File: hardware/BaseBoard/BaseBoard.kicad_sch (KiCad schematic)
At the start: 79 parts, among them IC1 PCF8574RGTR, J1-ESP1 ESP-1-L, J1-ESP2 ESP-1-L, J1-ESP3 ESP-1-L, J1-ESP4 ESP-1-L, J1-ESP5 ESP-1-L, J1-ESP6 ESP-1-L, J1-ESP7 ESP-1-L, J1-ESP8 ESP-1-L, J2-ESP1 ESP-1-R, J2-ESP2 ESP-1-R, J2-ESP3 ESP-1-R, J2-ESP4 ESP-1-R, J2-ESP5 ESP-1-R, J2-ESP6 ESP-1-R, J2-ESP7 ESP-1-R, J2-ESP8 ESP-1-R, J3-BUS1 BUS-IN, J3-BUS2 BUS-IN, J3-BUS3 BUS-IN, J3-BUS4 BUS-IN, J3-BUS5 BUS-IN, J3-BUS6 BUS-IN, J3-BUS7 BUS-IN, J3-BUS8 BUS-IN, J4-BUS1 BUS-OUT, J4-BUS2 BUS-OUT, J4-BUS3 BUS-OUT, J4-BUS4 BUS-OUT, J4-BUS5 BUS-OUT, J4-BUS6 BUS-OUT, J4-BUS7 BUS-OUT, J4-BUS8 BUS-OUT, Q1 AO3401A, Q2 AO3401A, Q3 AO3401A, Q4 AO3401A, Q5 AO3401A, Q6 AO3401A, Q7 AO3401A, Q8 AO3401A, SW1 SW_DIP_SPSTx03

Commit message: Larger resistors and more GND vias.
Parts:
- R11, R12, R21, R22, R31, R32, R41, R42, R51, R52, R61, R62, R71, R72, R81, R82: footprint Resistor_SMD:R_0402_1005Metric -> Resistor_SMD:R_0805_2012Metric
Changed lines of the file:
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@@
 			)
 		)
-		(property "Footprint" "Resistor_SMD:R_0402_1005Metric"
+		(property "Footprint" "Resistor_SMD:R_0805_2012Metric"
 			(at 66.548 77.47 90)
 			(effects
@@
 			)
 		)
-		(property "Footprint" "Resistor_SMD:R_0402_1005Metric"
+		(property "Footprint" "Resistor_SMD:R_0805_2012Metric"
 			(at 59.69 84.328 90)
 			(effects
@@
 			)
 		)
-		(property "Footprint" "Resistor_SMD:R_0402_1005Metric"
+		(property "Footprint" "Resistor_SMD:R_0805_2012Metric"
 			(at 130.81 44.958 90)
 			(effects
@@
 			)
 		)
-		(property "Footprint" "Resistor_SMD:R_0402_1005Metric"
+		(property "Footprint" "Resistor_SMD:R_0805_2012Metric"
 			(at 130.81 84.328 90)
 			(effects
@@
 			)
 		)
-		(property "Footprint" "Resistor_SMD:R_0402_1005Metric"
+		(property "Footprint" "Resistor_SMD:R_0805_2012Metric"
 			(at 59.69 44.958 90)
 			(effects
@@
 			)
 		)
-		(property "Footprint" "Resistor_SMD:R_0402_1005Metric"
+		(property "Footprint" "Resistor_SMD:R_0805_2012Metric"
 			(at 137.668 116.84 90)
 			(effects
@@
 			)
 		)
-		(property "Footprint" "Resistor_SMD:R_0402_1005Metric"
+		(property "Footprint" "Resistor_SMD:R_0805_2012Metric"
 			(at 130.81 123.698 90)
 			(effects
@@
 			)
 		)
-		(property "Footprint" "Resistor_SMD:R_0402_1005Metric"
+		(property "Footprint" "Resistor_SMD:R_0805_2012Metric"
 			(at 130.81 163.068 90)
 			(effects
@@
 			)
 		)
-		(property "Footprint" "Resistor_SMD:R_0402_1005Metric"
+		(property "Footprint" "Resistor_SMD:R_0805_2012Metric"
 			(at 59.69 123.698 90)
 			(effects
@@
 			)
 		)
-		(property "Footprint" "Resistor_SMD:R_0402_1005Metric"
+		(property "Footprint" "Resistor_SMD:R_0805_2012Metric"
 			(at 66.548 156.21 90)
 			(effects
@@
 			)
 		)
-		(property "Footprint" "Resistor_SMD:R_0402_1005Metric"
+		(property "Footprint" "Resistor_SMD:R_0805_2012Metric"
 			(at 66.548 38.1 90)
 			(effects
@@
 			)
 		)
-		(property "Footprint" "Resistor_SMD:R_0402_1005Metric"
+		(property "Footprint" "Resistor_SMD:R_0805_2012Metric"
 			(at 137.668 156.21 90)
 			(effects
@@
 			)
 		)
-		(property "Footprint" "Resistor_SMD:R_0402_1005Metric"
+		(property "Footprint" "Resistor_SMD:R_0805_2012Metric"
 			(at 59.69 163.068 90)
 			(effects
@@
 			)
 		)
-		(property "Footprint" "Resistor_SMD:R_0402_1005Metric"
+		(property "Footprint" "Resistor_SMD:R_0805_2012Metric"
 			(at 137.668 38.1 90)
 			(effects
@@
 			)
 		)
-		(property "Footprint" "Resistor_SMD:R_0402_1005Metric"
+		(property "Footprint" "Resistor_SMD:R_0805_2012Metric"
 			(at 137.668 77.47 90)
 			(effects
@@
 			)
 		)
-		(property "Footprint" "Resistor_SMD:R_0402_1005Metric"
+		(property "Footprint" "Resistor_SMD:R_0805_2012Metric"
 			(at 66.548 116.84 90)
 			(effects

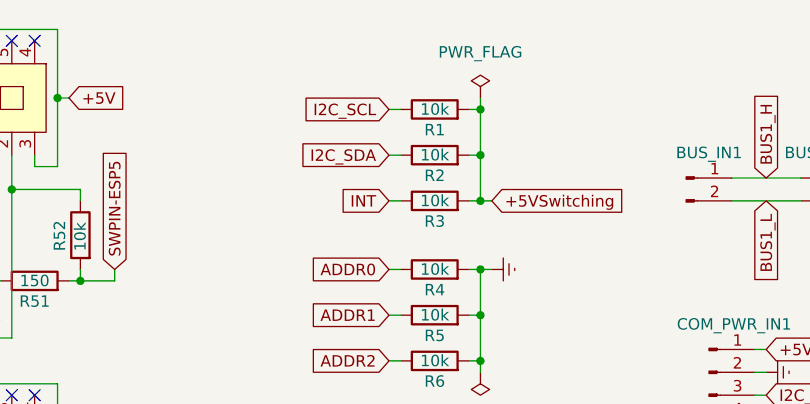
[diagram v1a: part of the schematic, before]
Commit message: Removed pull-up resistors for I2C slaves.
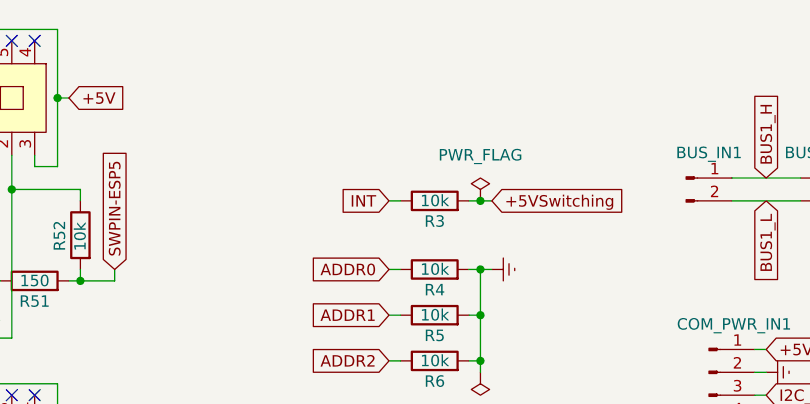
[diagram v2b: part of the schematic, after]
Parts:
- removed R1, R2: 10k, Resistor_SMD:R_0402_1005Metric, symbol Device:R

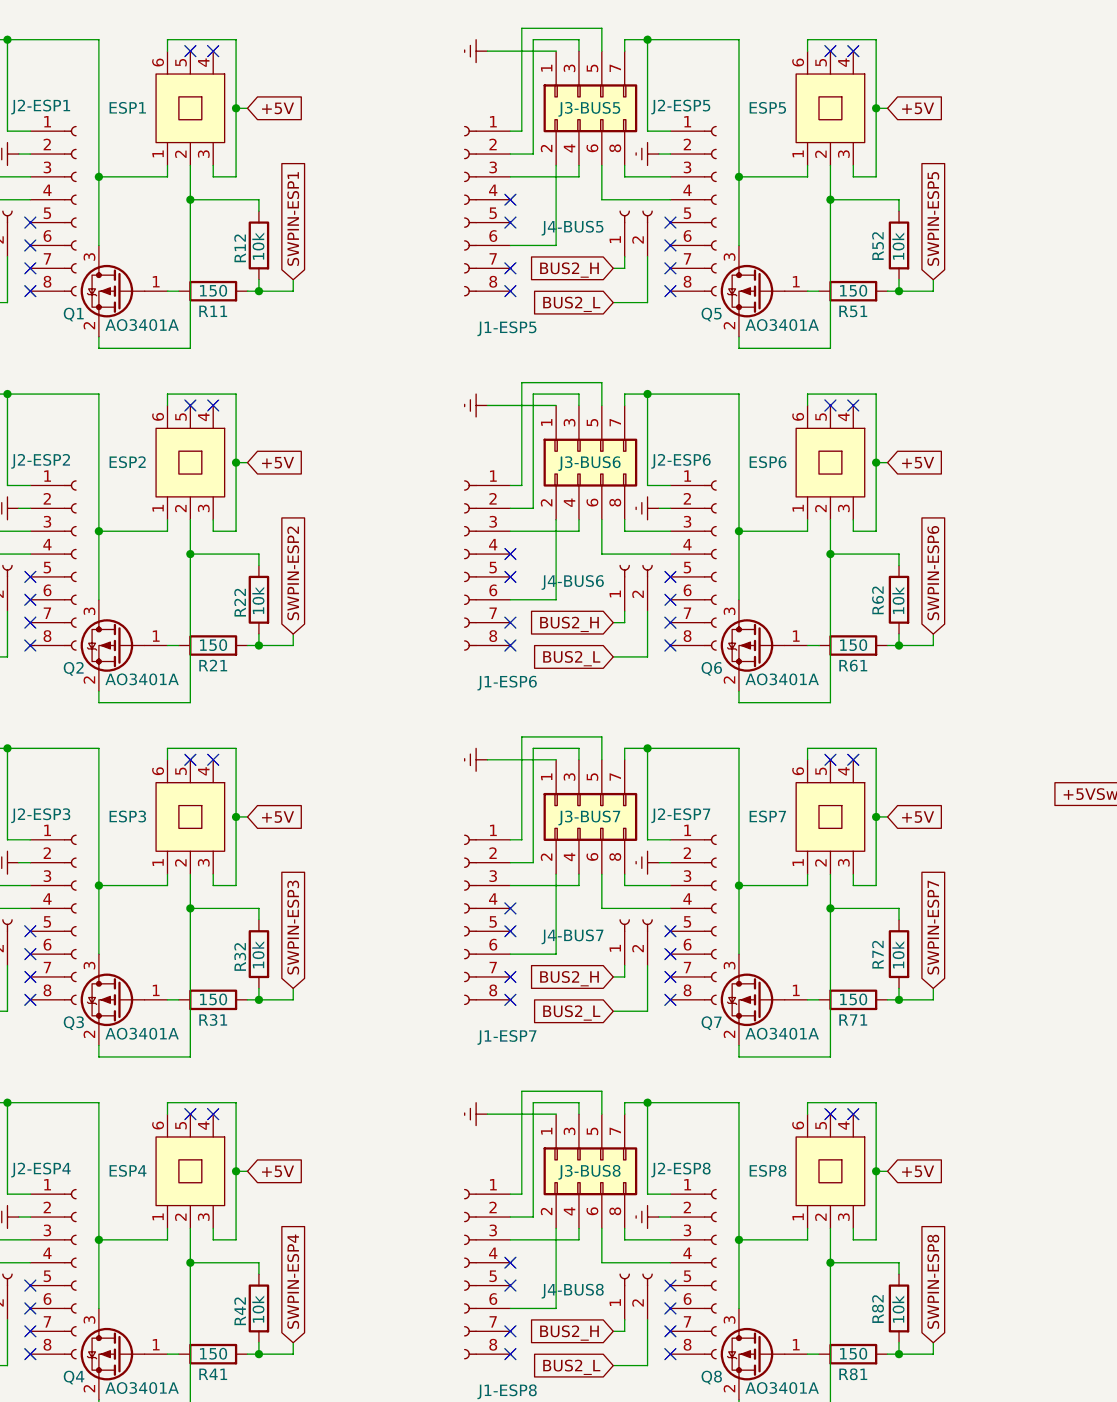
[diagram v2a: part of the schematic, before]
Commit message: Added diodes to base board.
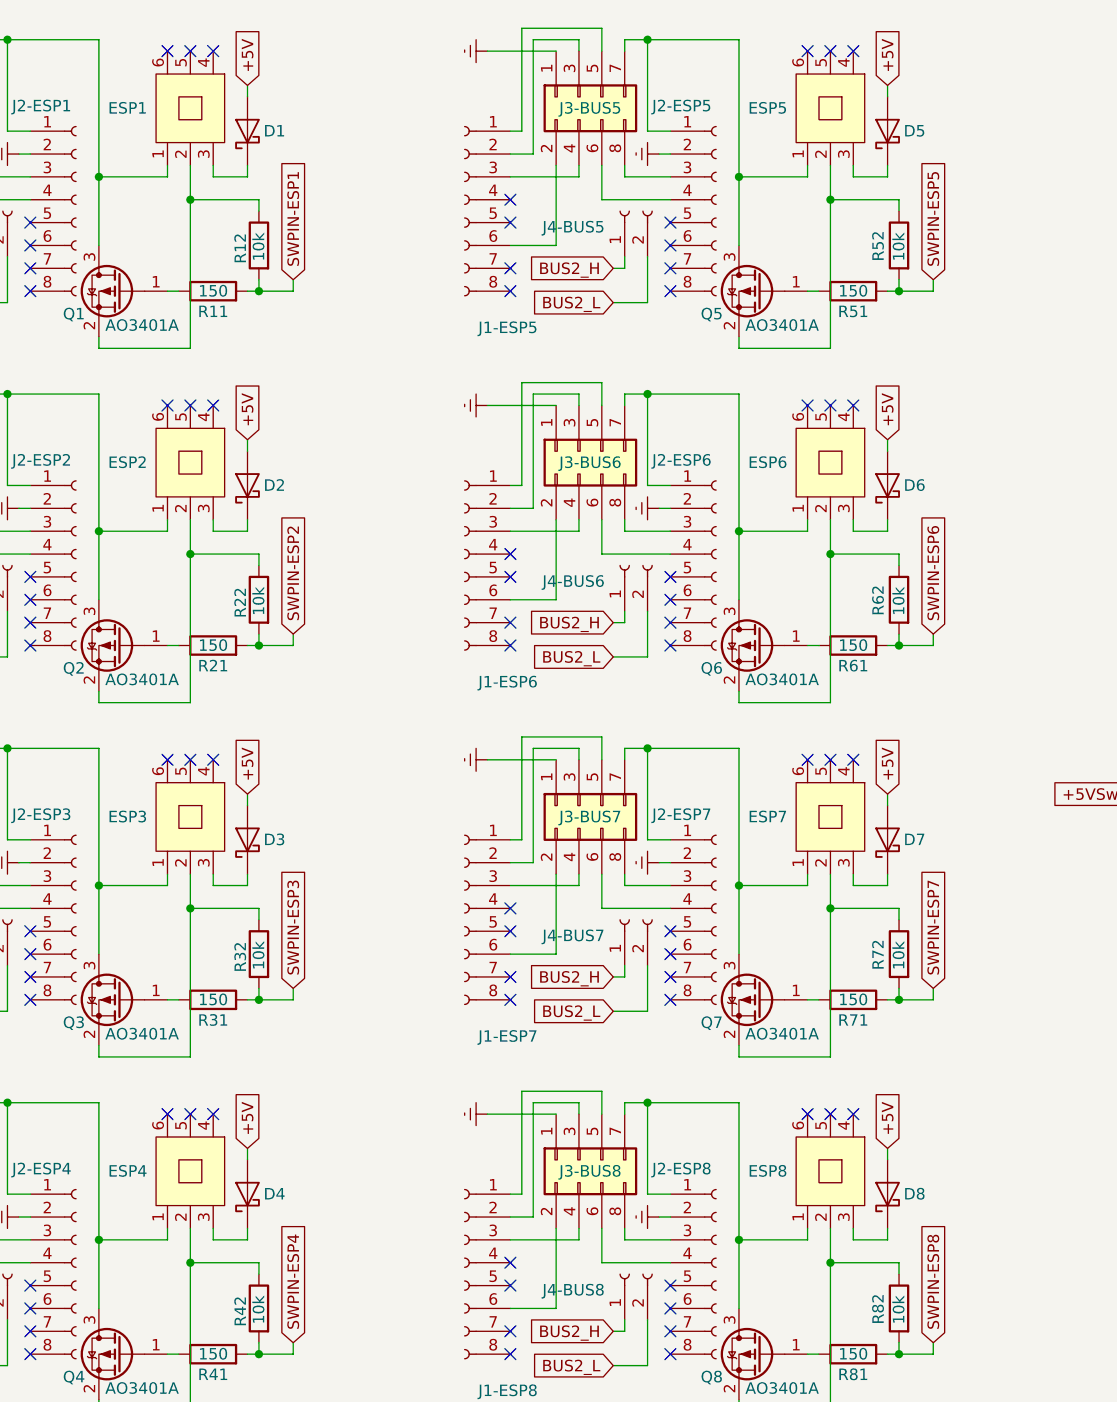
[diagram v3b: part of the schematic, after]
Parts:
- added D1, D2, D3, D4, D5, D6, D7, D8: MBR1020VL, Diode_SMD:D_SOD-123F, symbol Diode:MBR1020VL
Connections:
- net +5V: now also D1.2 (A), D2.2 (A), D3.2 (A), D4.2 (A), D5.2 (A), D6.2 (A), D7.2 (A), D8.2 (A); no longer ESP1.3, ESP1.6, ESP2.3, ESP2.6, ESP3.3, ESP3.6, ESP4.3, ESP4.6, ESP5.3, ESP5.6, ESP6.3, ESP6.6, ESP7.3, ESP7.6, ESP8.3, ESP8.6
- new net: D6.1 (K), ESP6.3
- new net: D1.1 (K), ESP1.3
- new net: D8.1 (K), ESP8.3
- new net: D5.1 (K), ESP5.3
- new net: D7.1 (K), ESP7.3
- new net: D4.1 (K), ESP4.3
- new net: D3.1 (K), ESP3.3
- new net: D2.1 (K), ESP2.3
- no-connect marks 80 -> 88

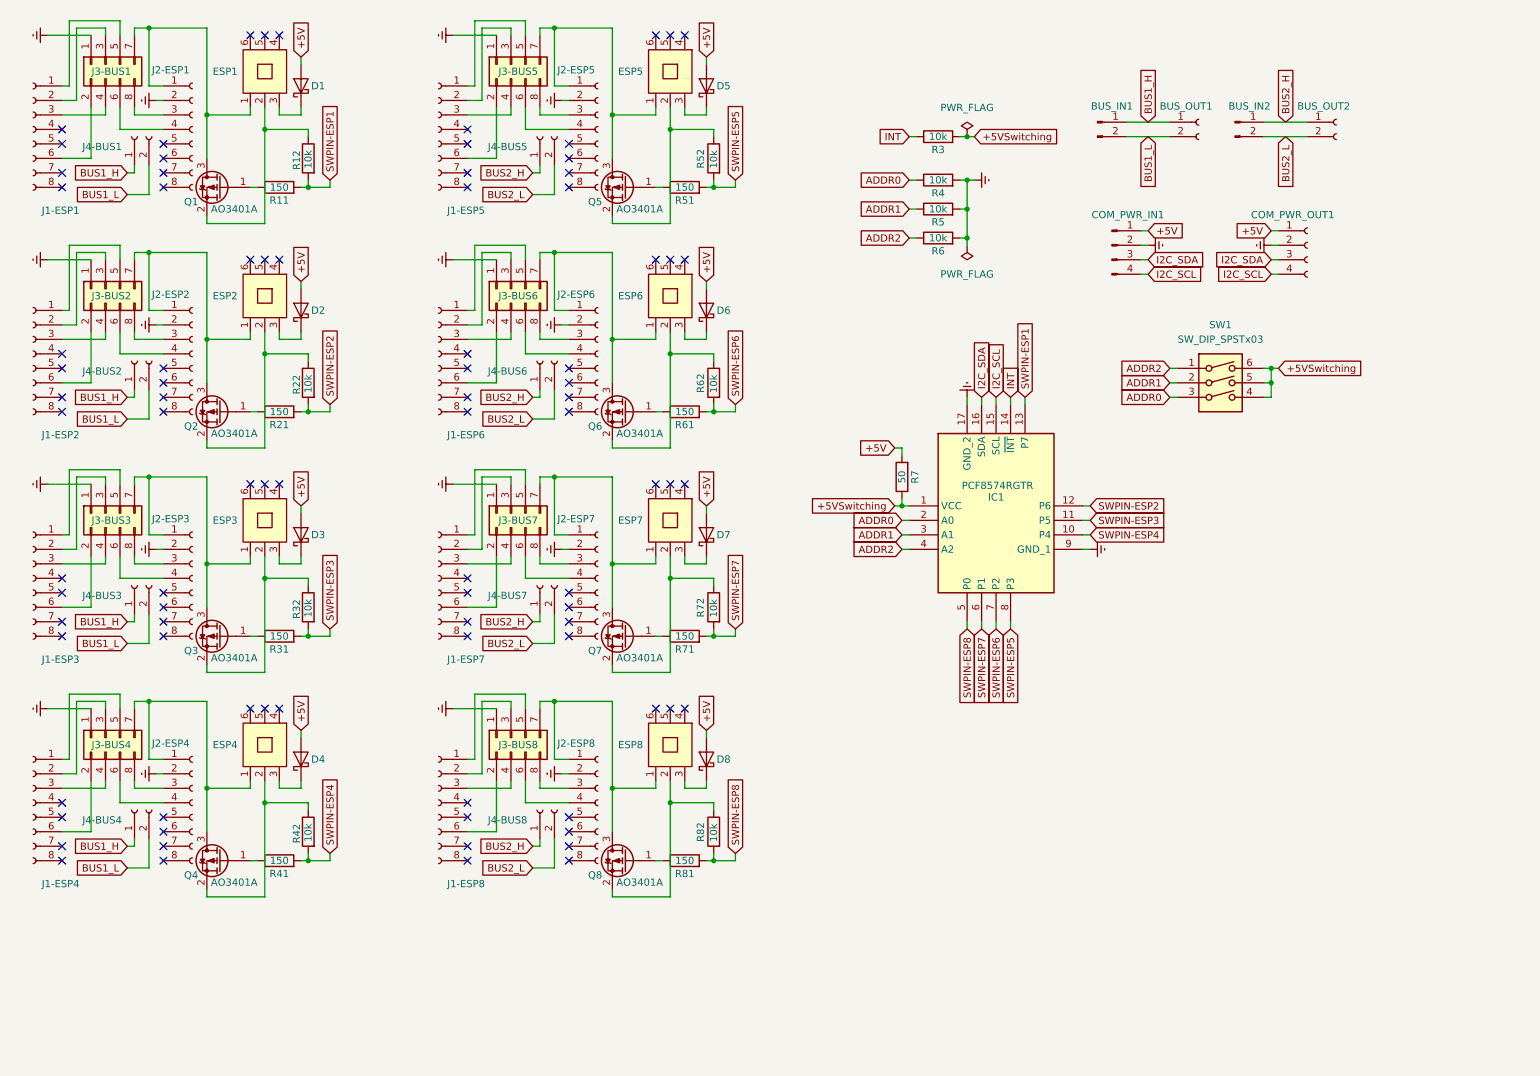
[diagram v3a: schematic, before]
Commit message: Added capacitors for +3V3 stabilization.
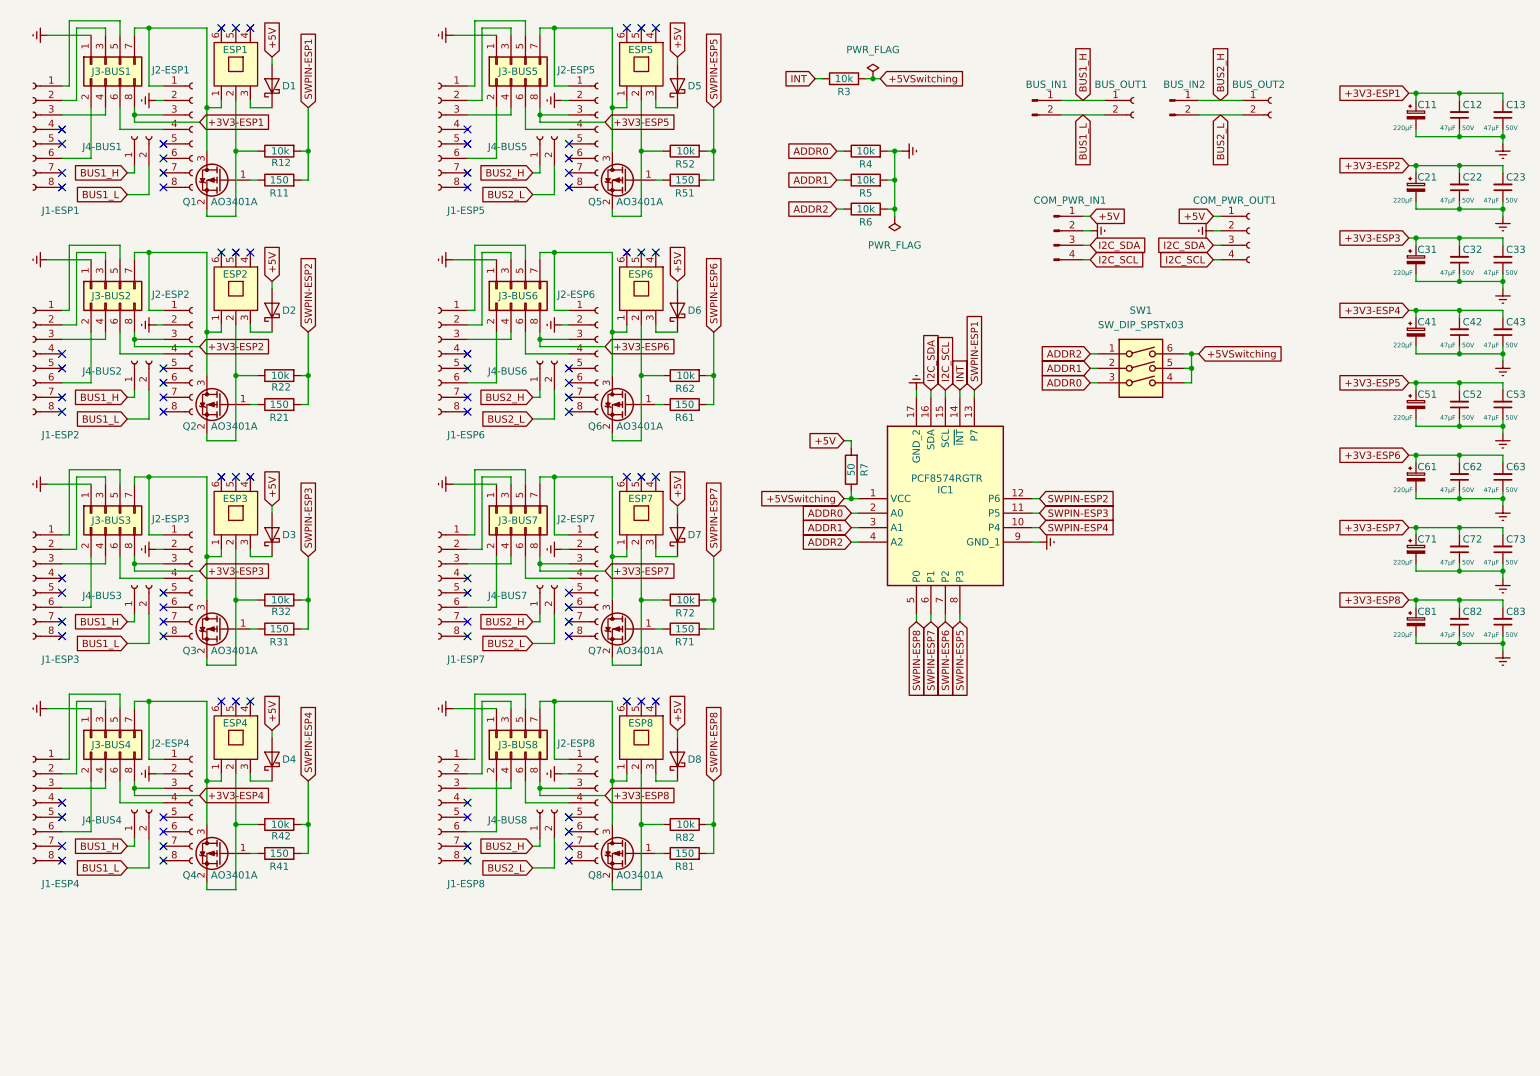
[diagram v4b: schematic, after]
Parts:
- added C11, C21, C31, C41, C51, C61, C71, C81: 220µF, Capacitor_SMD:CP_Elec_6.3x7.7, symbol Device:C_Polarized_Small
- added C12, C13, C22, C23, C32, C33, C42, C43, C52, C53, C62, C63, C72, C73, C82, C83: 47µF, Capacitor_SMD:C_0805_2012Metric, symbol Device:C_Small
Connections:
- net GNDREF: now also C11.2, C12.1, C13.1, C21.2, C22.1, C23.1, C31.2, C32.1, C33.1, C41.2, C42.1, C43.1, C51.2, C52.1, C53.1, C61.2, C62.1, C63.1, C71.2, C72.1, C73.1, C81.2, C82.1, C83.1
- net +3V3-ESP7: now reaches J2-ESP7.3 (Pin_3), J3-BUS7.8 (Pin_8)
- net +3V3-ESP7: now also C71.1, C72.2, C73.2
- net +3V3-ESP4: now reaches J2-ESP4.3 (Pin_3), J3-BUS4.8 (Pin_8)
- net +3V3-ESP4: now also C41.1, C42.2, C43.2
- net +3V3-ESP2: now reaches J2-ESP2.3 (Pin_3), J3-BUS2.8 (Pin_8)
- net +3V3-ESP2: now also C21.1, C22.2, C23.2
- net +3V3-ESP8: now reaches J2-ESP8.3 (Pin_3), J3-BUS8.8 (Pin_8)
- net +3V3-ESP8: now also C81.1, C82.2, C83.2
- net +3V3-ESP1: now reaches J2-ESP1.3 (Pin_3), J3-BUS1.8 (Pin_8)
- net +3V3-ESP1: now also C11.1, C12.2, C13.2
- net +3V3-ESP3: now reaches J2-ESP3.3 (Pin_3), J3-BUS3.8 (Pin_8)
- net +3V3-ESP3: now also C31.1, C32.2, C33.2
- net +3V3-ESP6: now reaches J2-ESP6.3 (Pin_3), J3-BUS6.8 (Pin_8)
- net +3V3-ESP6: now also C61.1, C62.2, C63.2
- net +3V3-ESP5: now reaches J2-ESP5.3 (Pin_3), J3-BUS5.8 (Pin_8)
- net +3V3-ESP5: now also C51.1, C52.2, C53.2
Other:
- moved on the sheet: BUS_IN1, BUS_IN2, BUS_OUT1, BUS_OUT2, COM_PWR_IN1, COM_PWR_OUT1, D1, D2, D3, D4, D5, D6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
